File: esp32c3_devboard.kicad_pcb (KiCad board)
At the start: 4 copper layers, 60 x 34 mm, 69 parts, among them J1 USB_C_Receptacle_USB2.0, J2 Conn_01x15_Male, J3 Conn_01x15_Male, Q1 S8050, Q2 S8050, SW1 BOOT, SW2 RST, U1 AMS1117-3.3, U2 SRV05-4, U3 USB2514B_Bi, U4 CP2102N-A01-GQFN28, U5 ESP32-C3-WROOM-02-SOCKET, Y1 24MHz

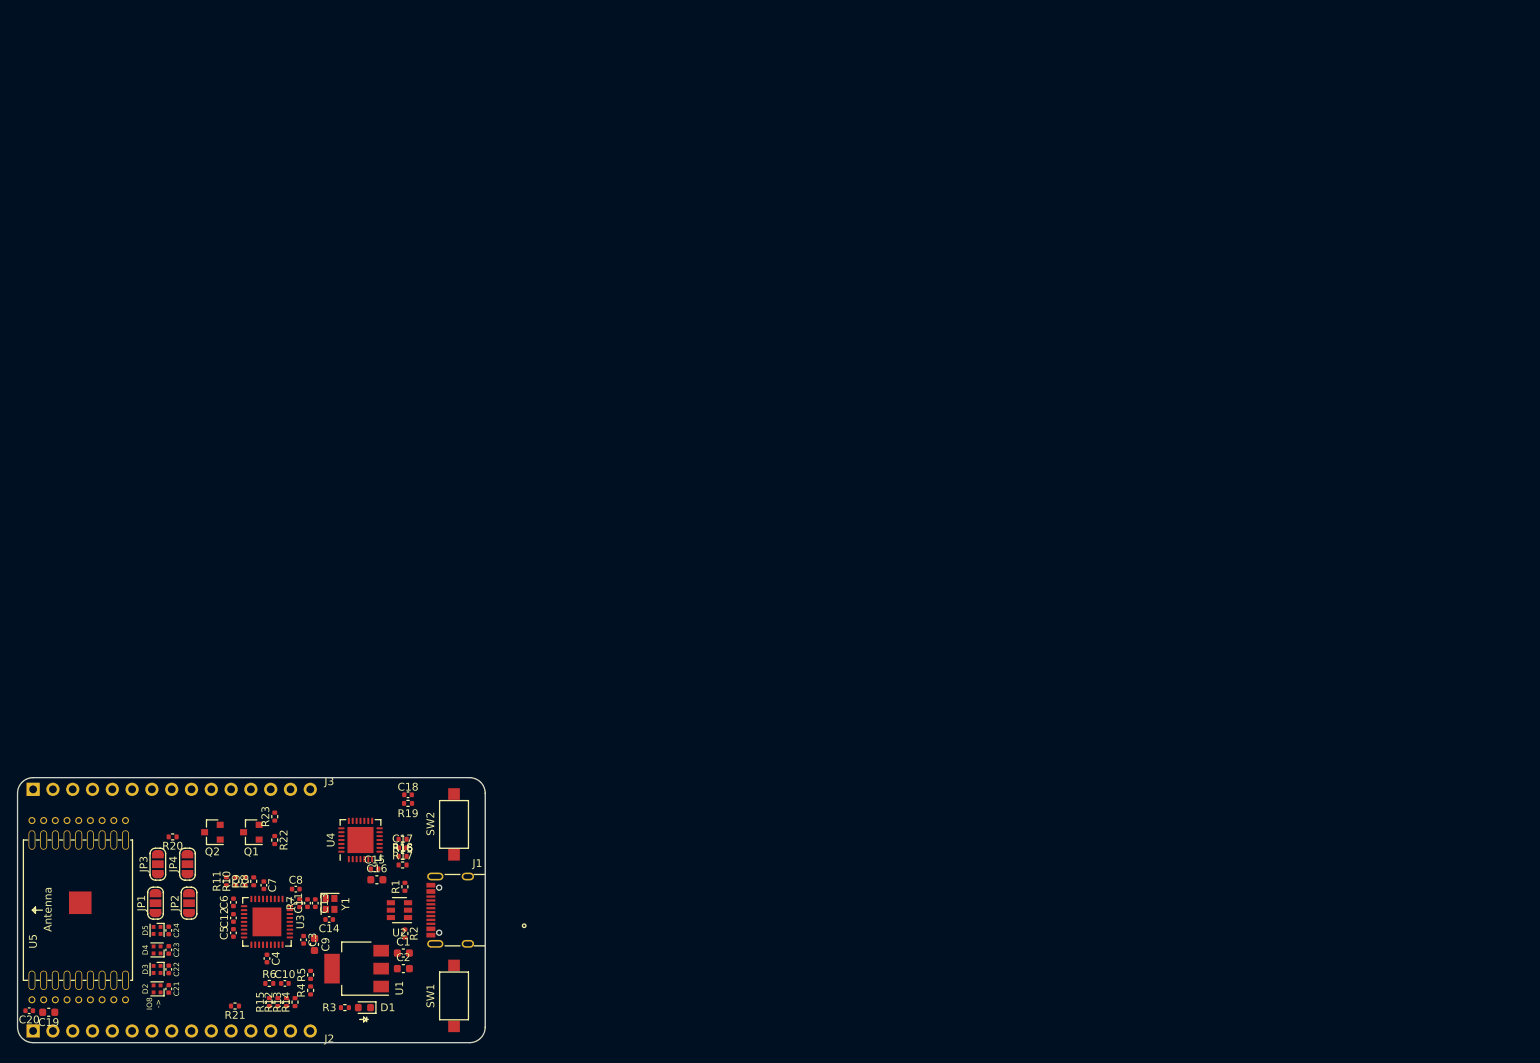
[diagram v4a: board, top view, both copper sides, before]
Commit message: PCB: Routing done
Signed-off-by: Tomislav Milkovic <tomislav.milkovic95@gmail.com>
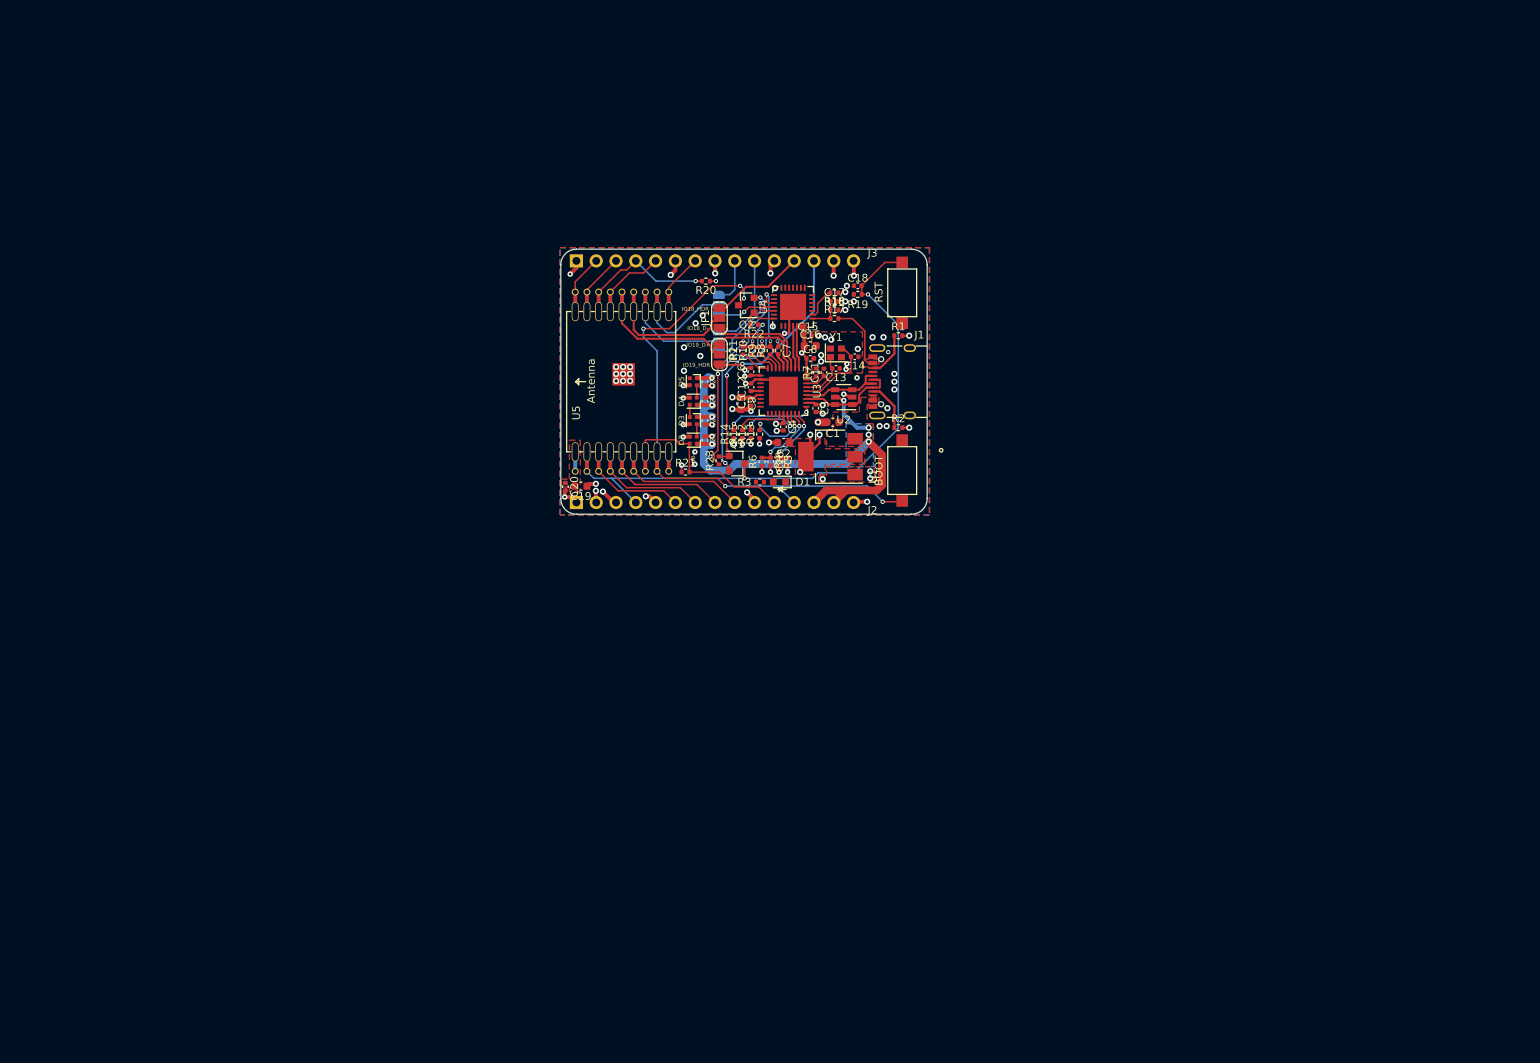
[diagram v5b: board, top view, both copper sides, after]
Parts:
- JP3, JP4: moved to B.Cu
- moved JP1 104.3 mm to (135.1, 90.0)
- moved JP3 101.6 mm to (135.0, 88.3)
- moved R20 98.8 mm to (133.3, 85.3)
- moved C14 98.8 mm to (152.4, 95.0)
- moved C21 98.4 mm to (133.2, 105.7)
- moved C22 98.4 mm to (133.2, 103.2)
- moved C23 98.4 mm to (133.2, 100.7)
- moved C24 98.4 mm to (133.2, 98.2)
- moved D2 98.4 mm to (131.7, 105.7)
- moved D3 98.4 mm to (131.7, 103.2)
- moved D4 98.4 mm to (131.7, 100.7)
- moved D5 98.4 mm to (131.7, 98.2)
- moved JP2 97.9 mm to (135.1, 94.7), turned to 270 degrees
- moved J2 97.2 mm to (116.7, 113.7)
- moved J3 97.2 mm to (116.7, 82.7)
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- renumbered SW1 to BOOT, SW2 to RST
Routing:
- net +5V: track 0.00 -> 81.8 mm, vias 0 -> 9
- net /ESP32-C3 module/~RST: track 0.00 -> 78.9 mm, vias 0 -> 2
- net /ESP32-C3 module/GPIO9: track 0.00 -> 72.8 mm, vias 0 -> 5
- net GND: track 0.00 -> 55.2 mm, vias 0 -> 78
- net +3V3: track 0.00 -> 47.8 mm, vias 0 -> 22
- net /ESP32-C3 module/ESP32_UART_RTS: track 0.00 -> 27.5 mm, vias 0 -> 2
- net /ESP32-C3 module/GPIO8: track 0.00 -> 26.1 mm
- net Net-(Q2-Pad2): track 0.00 -> 25.7 mm, vias 0 -> 2
- net Net-(Q1-Pad2): track 0.00 -> 22.9 mm, vias 0 -> 2
- net /ESP32-C3 module/GPIO19_HEADER: track 0.00 -> 21.4 mm, vias 0 -> 1
- net /ESP32-C3 module/GPIO2: track 0.00 -> 18.5 mm, vias 0 -> 1
- net /ESP32-C3 module/GPIO19: track 0.00 -> 18.5 mm
- net /ESP32-C3 module/GPIO18: track 0.00 -> 17.4 mm
- net /ESP32-C3 module/GPIO7: track 0.00 -> 17.1 mm
- net /ESP32-C3 module/GPIO6: track 0.00 -> 16.1 mm
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- added copper zone on B.Cu, net +3V3
- added copper zone on F.Cu, net +3V3
- added copper zone on In2.Cu, net +3V3
- added copper zone on B.Cu, net +5V
- added copper zone on F.Cu, net +5V
- added copper zone on F.Cu, net GND
- added copper zone on In1.Cu, net GND
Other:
- board size 60 x 34 mm -> 47 x 34 mm
- rule via_min_drill: 0.3 -> 0.2
- rule via_min_size: 0.5 -> 0.35
- board text added: "IO18_D-"
- board text added: "IO18_HDR"
- board text added: "IO19_D+"
- board text added: "IO19_HDR"
- board text added: "IO20_HDR"
- board text added: "IO20_RXD"
- board text added: "IO21_HDR"
- board text added: "IO21_TXD"
- board text added: "IO8->"
- board text removed: "IO8 ->"

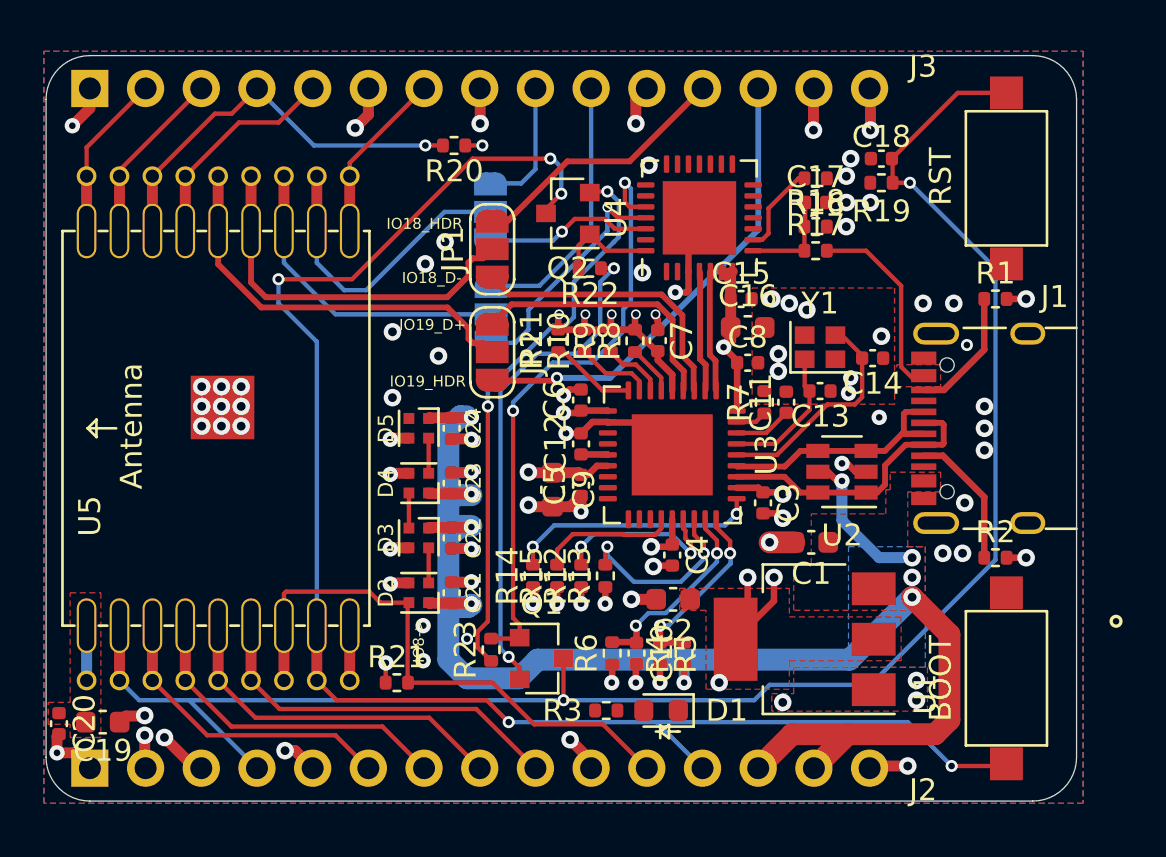
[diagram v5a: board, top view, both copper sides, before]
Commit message: Add fiducials, finish routing
Signed-off-by: Tomislav Milkovic <tomislav.milkovic95@gmail.com>
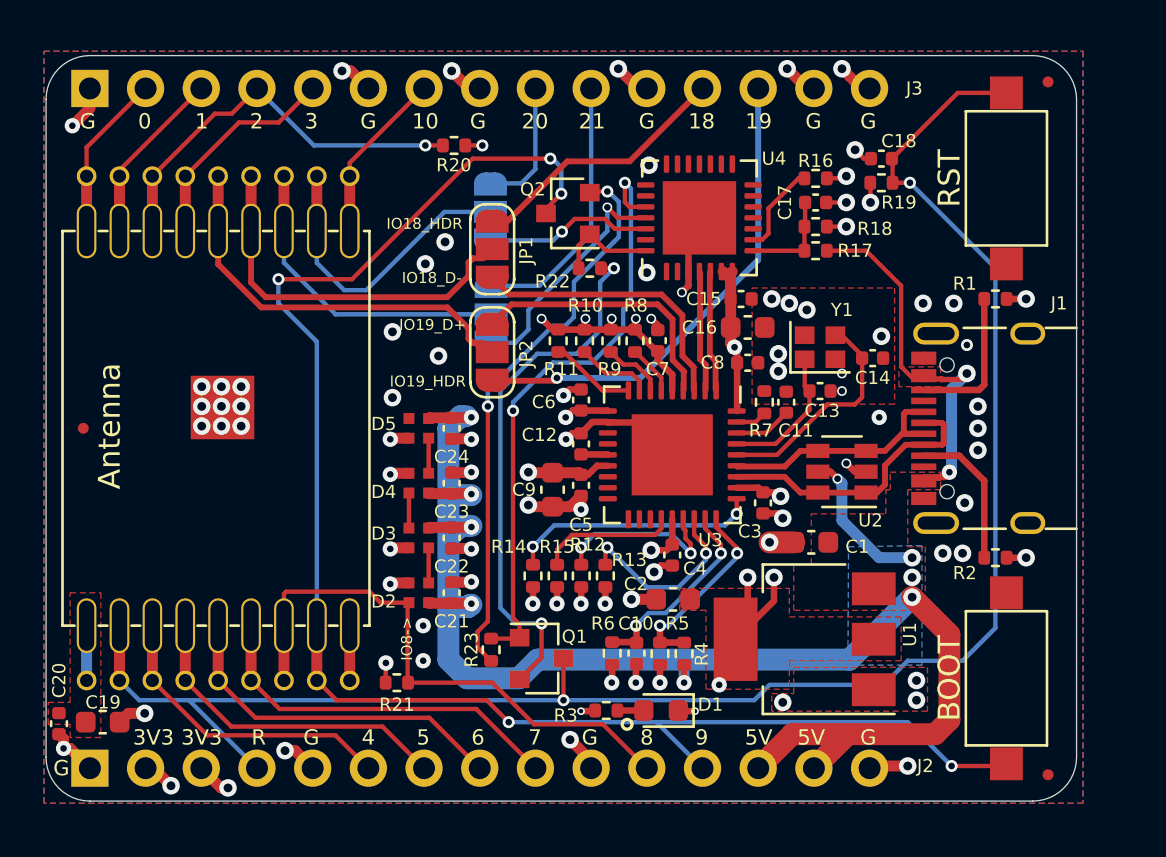
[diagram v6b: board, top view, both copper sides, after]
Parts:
- added FID1: Fiducial, Fiducial:Fiducial_0.5mm_Mask1mm, F.Cu at (160.4, 82.4)
- added FID2: Fiducial, Fiducial:Fiducial_0.5mm_Mask1mm, F.Cu at (160.4, 114.0)
- added FID3: Fiducial, Fiducial:Fiducial_0.5mm_Mask1mm, F.Cu at (116.4, 98.2)
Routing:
- net +5V: track 81.8 -> 90.4 mm, vias 9 -> 11
- net GND: track 55.2 -> 57.1 mm, vias 78 -> 79
- net /ESP32-C3 module/~RST: track 78.9 -> 80.8 mm
- net Net-(Q1-Pad2): track 22.9 -> 24.4 mm
- net +3V3: track 47.8 -> 46.5 mm
- net /USB connector and power supply/PWR_LED_A: track 0.00 -> 1.20 mm
- net Net-(J1-PadB5): track 5.83 -> 6.77 mm
- net /ESP32-C3 module/GPIO19_HEADER: track 21.4 -> 22.2 mm
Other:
- net class Default: clearance 0.2 -> 0.1
- rule trace_clearance: 0.2 -> 0.1
- board text added: "0"
- board text added: "1"
- board text added: "10"
- board text added: "18"
- board text added: "19"
- board text added: "2"
- board text added: "20"
- board text added: "21"
- board text added: "3"
- board text added: "3V3"
- board text added: "4"
- board text added: "5"
- board text added: "5V"
- board text added: "6"
- board text added: "7"
- board text added: "8"
- board text added: "9"
- board text added: "G"
- board text added: "R"
